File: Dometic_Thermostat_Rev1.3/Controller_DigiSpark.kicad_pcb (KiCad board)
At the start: 2 copper layers, 82.3 x 63.2 mm, 31 parts, among them P1 UNREG_12V_IN, P2 UNUSED_MICRO_PINS, P3 RELAY_SW_OUT, P4 RELAY_NC, P5 FUSE_BLOCK, P6 AUX_VOLT_CONN, Q1 2N3904, Q2 2N2222A, T1 Relay_SPDT, U1 7805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

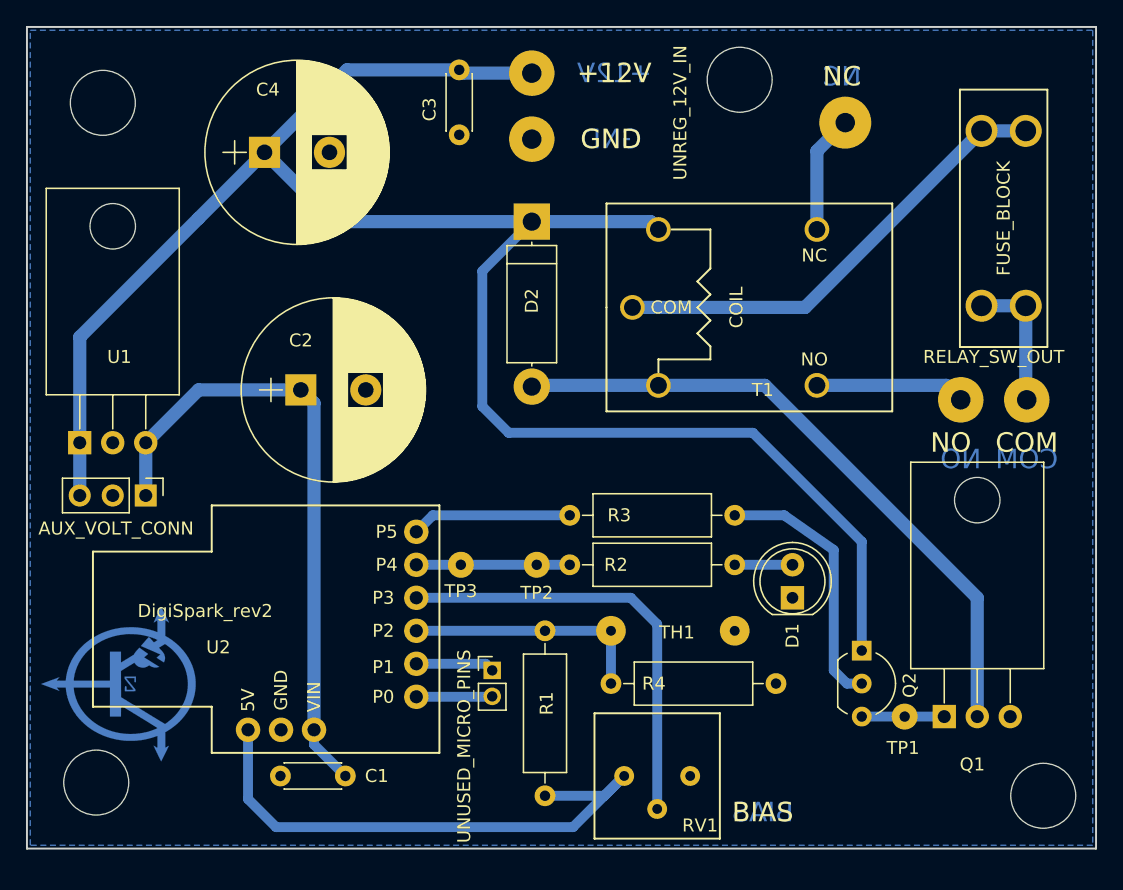
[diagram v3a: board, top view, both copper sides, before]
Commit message: Changed PCB-updated pin assg & added mount holes
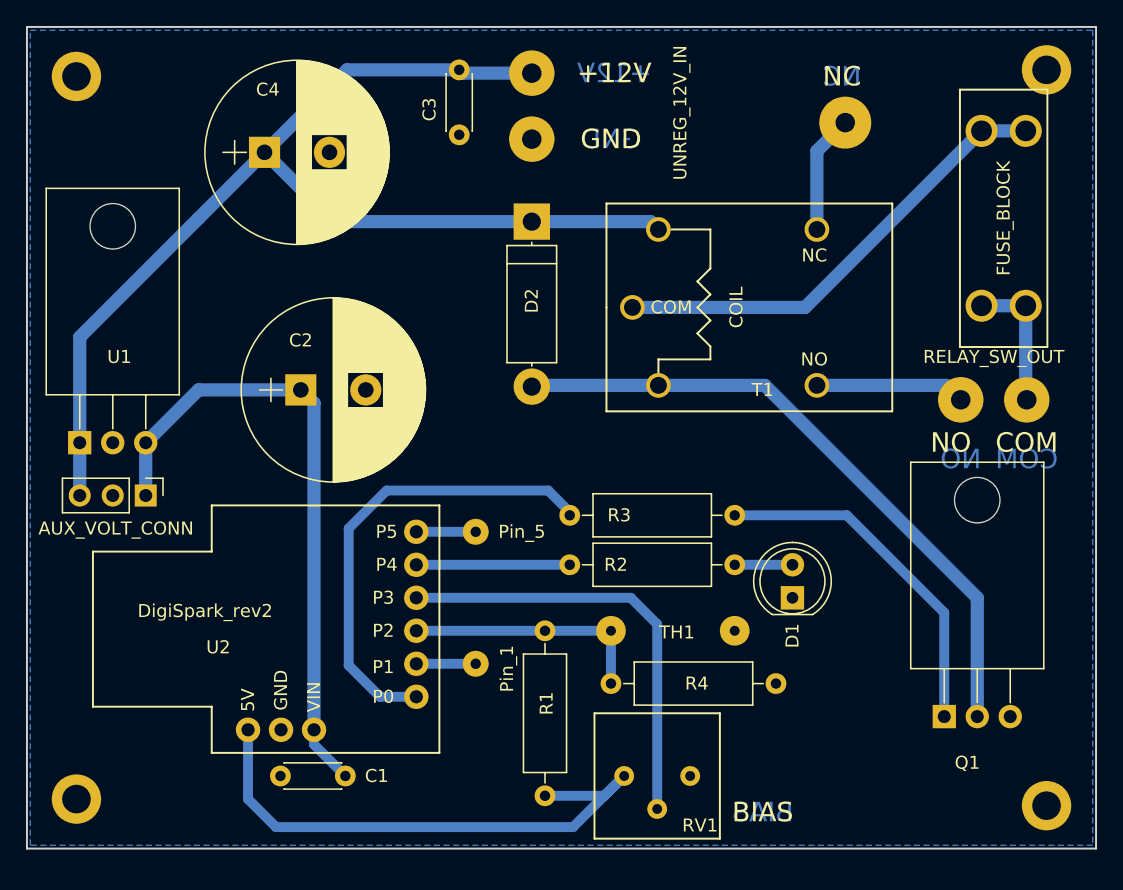
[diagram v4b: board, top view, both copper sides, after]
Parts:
- removed ?: LOGO, COMPLIB:LOGO_0-5IN_FCu
- removed P2: UNUSED_MICRO_PINS, Pin_Headers:Pin_Header_Straight_1x02_Pitch2.00mm
- removed Q2: 2N2222A, TO_SOT_Packages_THT:TO-92_Inline_Wide
- removed the REF** at (233.4, 106.9)
- removed the REF** at (256.8, 162.1)
- removed the REF** at (183.9, 161.0)
- removed the REF** at (184.4, 108.7)
- removed TP1, TP2, TP3: SolderWirePad_single_0-8mmDrill, Wire_Pads:SolderWirePad_single_0-8mmDrill
- added P7: Pin_1, Wire_Pads:SolderWirePad_single_0-8mmDrill, F.Cu at (213.1, 151.9)
- added P8: Pin_5, Wire_Pads:SolderWirePad_single_0-8mmDrill, F.Cu at (213.1, 141.7)
- added REF**: MountingHole_2.2mm_M2_DIN965_Pad, Mounting_Holes:MountingHole_2.2mm_M2_DIN965_Pad, F.Cu at (257.0, 162.8)
- added REF**: MountingHole_2.2mm_M2_DIN965_Pad, Mounting_Holes:MountingHole_2.2mm_M2_DIN965_Pad, F.Cu at (182.4, 106.7)
- added REF**: MountingHole_2.2mm_M2_DIN965_Pad, Mounting_Holes:MountingHole_2.2mm_M2_DIN965_Pad, F.Cu at (257.0, 106.2)
- added REF**: MountingHole_2.2mm_M2_DIN965_Pad, Mounting_Holes:MountingHole_2.2mm_M2_DIN965_Pad, F.Cu at (182.4, 162.3)
- Q1: value 2N3904 -> IRF_3205
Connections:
- R3 pad 1: Net-(Q2-Pad2) -> Net-(Q1-Pad1)
- U2 pad 0: Net-(P2-Pad2) -> Net-(R3-Pad2)
- U2 pad 5: Net-(R3-Pad2) -> Net-(P8-Pad1)
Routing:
- net +12V: track 147.3 -> 89.6 mm
- net Net-(R3-Pad2): track 12.8 -> 35.9 mm
- net Net-(Q1-Pad1): track 6.35 -> 27.2 mm
- net Net-(Q2-Pad2): track 20.4 -> 0.00 mm
- net Net-(P2-Pad2): track 6.66 -> 0.00 mm
- net Net-(P8-Pad1): track 0.00 -> 5.08 mm
- net Net-(P7-Pad1): track 6.41 -> 4.57 mm
